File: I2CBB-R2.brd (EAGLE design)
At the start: 39.4 x 19.2 mm, 17 parts, among them IC1 74LVC1G07DBV, IC2 24AA64T, IC3 MCP1700T, IC4 MCP3221, IC5 SC18IS602, IC6 PCA9665

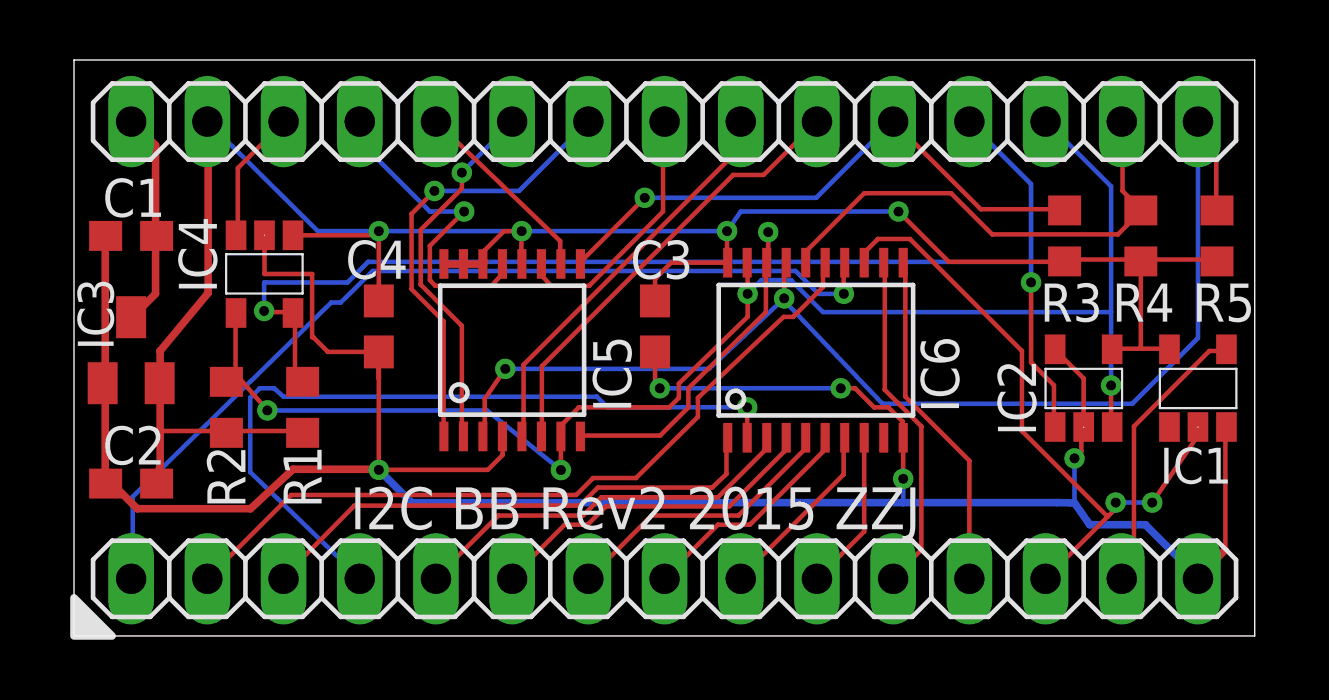
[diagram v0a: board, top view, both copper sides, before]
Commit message: Better trace routing on ADC
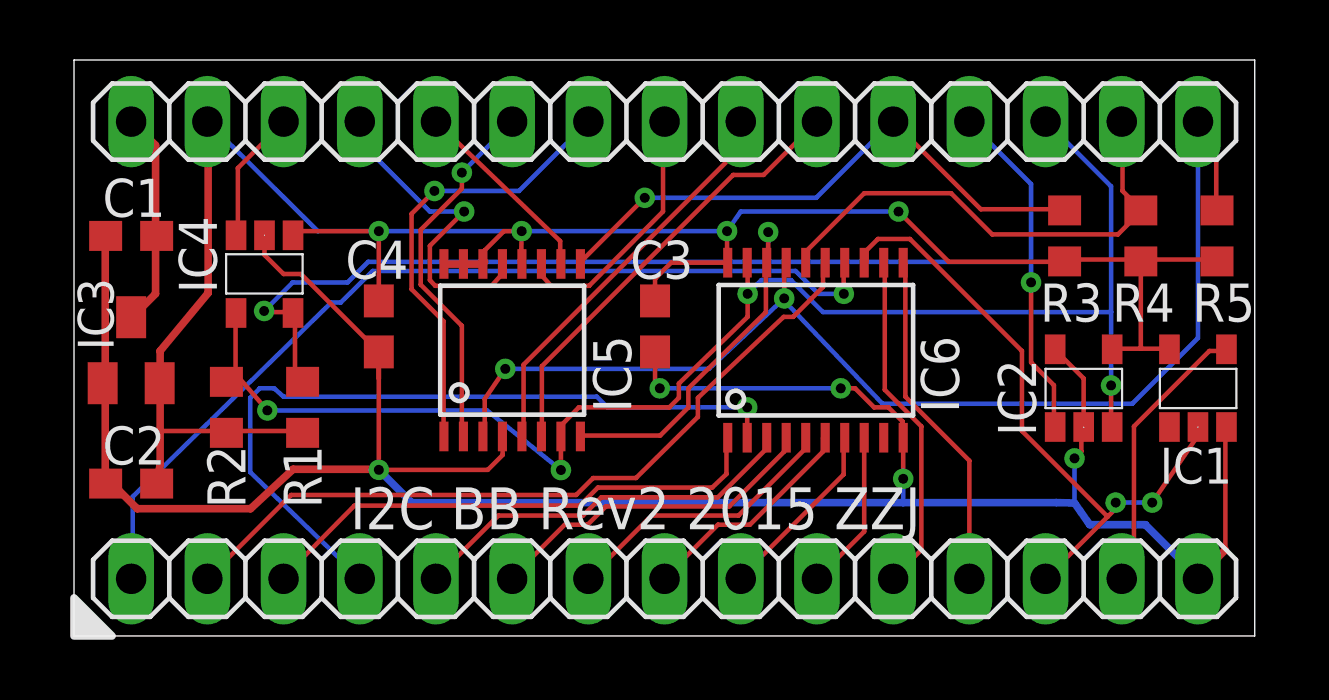
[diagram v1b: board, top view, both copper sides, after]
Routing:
- net GND: track 88.4 -> 86.8 mm
- net SCL: track 53.6 -> 53.0 mm
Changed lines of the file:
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@@
 <wire x1="28.275" y1="7.2422" x2="28.275" y2="5.87375" width="0.1524" layer="1"/>
 <wire x1="28.275" y1="5.87375" x2="28.275" y2="5.08" width="0.1524" layer="16"/>
-<wire x1="10.795" y1="10.10375" x2="9.09865" y2="10.10375" width="0.1524" layer="1"/>
-<wire x1="9.09865" y1="10.10375" x2="8.6106" y2="10.5918" width="0.1524" layer="1"/>
-<wire x1="8.6106" y1="10.5918" x2="8.5725" y2="10.5918" width="0.1524" layer="1"/>
-<wire x1="8.5725" y1="10.5918" x2="8.5725" y2="12.7" width="0.1524" layer="1"/>
-<wire x1="8.5725" y1="12.7" x2="6.985" y2="12.7" width="0.1524" layer="1"/>
-<wire x1="6.985" y1="12.7" x2="6.985" y2="13.99" width="0.1524" layer="1"/>
+<wire x1="6.985" y1="13.99" x2="6.985" y2="13.335" width="0.1524" layer="1"/>
+<wire x1="6.985" y1="13.335" x2="7.62" y2="12.7" width="0.1524" layer="1"/>
+<wire x1="7.62" y1="12.7" x2="8.19875" y2="12.7" width="0.1524" layer="1"/>
+<wire x1="8.19875" y1="12.7" x2="10.795" y2="10.10375" width="0.1524" layer="1"/>
 </signal>
 <signal name="VCC" class="1">
@@
 <wire x1="14.3256" y1="13.4874" x2="14.96695" y2="14.12875" width="0.1524" layer="1"/>
 <wire x1="14.96695" y1="14.12875" x2="15.5575" y2="14.12875" width="0.1524" layer="1"/>
-<wire x1="7.935" y1="13.99" x2="10.795" y2="13.99" width="0.1524" layer="1"/>
-<wire x1="10.795" y1="13.99" x2="10.795" y2="14.12875" width="0.1524" layer="1"/>
+<wire x1="10.795" y1="14.12875" x2="8.07375" y2="14.12875" width="0.1524" layer="1"/>
+<wire x1="8.07375" y1="14.12875" x2="7.935" y2="13.99" width="0.1524" layer="1"/>
 </signal>
 <signal name="SDA">
@@
 <wire x1="21.11375" y1="8.255" x2="21.11375" y2="8.89" width="0.1524" layer="1"/>
 <wire x1="21.11375" y1="8.89" x2="23.6982" y2="11.43" width="0.1524" layer="1"/>
-<wire x1="9.7536" y1="12.4206" x2="6.985" y2="12.4206" width="0.1524" layer="16"/>
-<wire x1="6.985" y1="12.4206" x2="6.985" y2="12.3825" width="0.1524" layer="16"/>
-<wire x1="6.985" y1="12.3825" x2="6.9723" y2="12.3825" width="0.1524" layer="16"/>
-<wire x1="6.9723" y1="12.3825" x2="6.9723" y2="11.4681" width="0.1524" layer="16"/>
 <wire x1="7.76605" y1="11.43" x2="6.9723" y2="11.43" width="0.1524" layer="1"/>
 <wire x1="6.9723" y1="11.43" x2="6.9723" y2="11.4681" width="0.1524" layer="1"/>
+<wire x1="9.7536" y1="12.4206" x2="7.9248" y2="12.4206" width="0.1524" layer="16"/>
+<wire x1="7.9248" y1="12.4206" x2="6.9723" y2="11.4681" width="0.1524" layer="16"/>
 </signal>
 <signal name="N$1">
